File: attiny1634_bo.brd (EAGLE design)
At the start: 49.5 x 22.2 mm, 11 parts, among them J1 AVR_SPI_PRG_6NS, Y1 16MHz

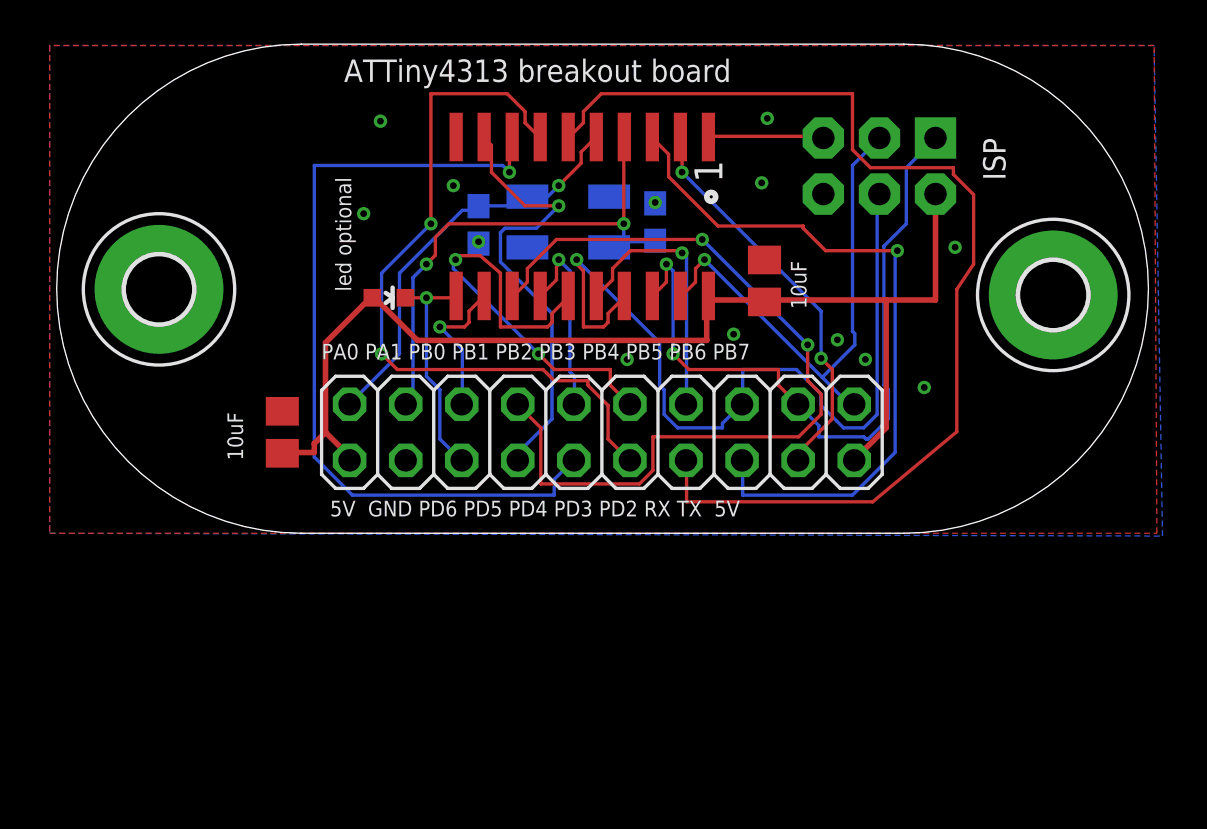
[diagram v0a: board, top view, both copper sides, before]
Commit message: use the new part and remove old wires from schematic
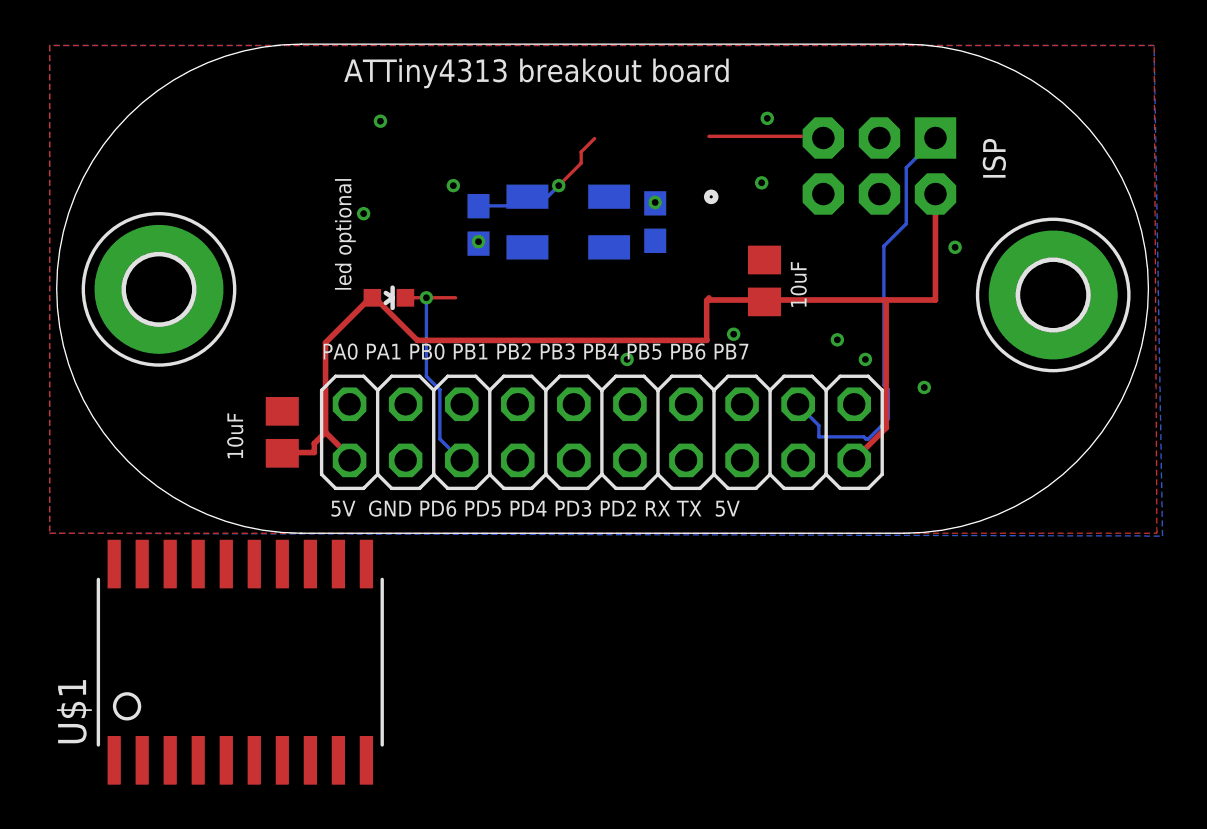
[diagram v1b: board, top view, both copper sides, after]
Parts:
- U$1: value ATTINY2313A -> ATTINY1634; device SparkFun-DigitalIC:SOP20 -> attiny1634:SOIC20
- moved U$1 36.0 mm to (-0.25, -12.2), turned to 0 degrees
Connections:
- removed net PA0/XTAL1: CX0.2, JP1.19, U$1.5, Y1.3
- removed net PA1/XTAL2: CX1.2, JP1.17, U$1.4, Y1.1
- removed net PA2/RESET-: J1.5, U$1.1
- removed net PB0: JP1.15, U$1.12
- removed net PB1: JP1.13, U$1.13
- removed net PB2: JP1.11, U$1.14
- removed net PB3: JP1.9, U$1.15
- removed net PB4: JP1.7, U$1.16
- removed net PB5/MOSI: J1.4, JP1.5, U$1.17
- removed net PB7/SCL: J1.3, JP1.1, U$1.19
- removed net PD0/RDX: JP1.4, U$1.2
- removed net PD1/TXD: JP1.6, U$1.3
- removed net PD2: JP1.8, U$1.6
- removed net PD3: JP1.10, U$1.7
- removed net PD4: JP1.12, U$1.8
- removed net PD5: JP1.14, U$1.9
- new net N$11: CX0.2, Y1.3
- new net N$3: J1.5
- new net N$4: J1.4
- new net N$7: J1.3
- new net N$9: CX1.2, Y1.1
- new net VCC: U$1.11
- net +5V: no longer U$1.20
- net PB6/MISO: no longer JP1.3, U$1.18
- net PD6: no longer JP1.16, U$1.11
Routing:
- net PD2: track 49.3 -> 0.00 mm
- net PB1: track 39.1 -> 0.00 mm, vias 2 -> 0
- net PB5/MOSI: track 38.2 -> 0.00 mm, vias 1 -> 0
- net PD4: track 37.4 -> 0.00 mm, vias 1 -> 0
- net PD3: track 33.0 -> 0.00 mm, vias 2 -> 0
- net PD1/TXD: track 32.4 -> 0.00 mm, vias 1 -> 0
- net PA1/XTAL2: track 24.7 -> 0.00 mm, vias 2 -> 0
- net PB7/SCL: track 23.6 -> 0.00 mm, vias 1 -> 0
- net PD5: track 20.5 -> 0.00 mm, vias 1 -> 0
- net PB3: track 20.3 -> 0.00 mm, vias 2 -> 0
- net PA0/XTAL1: track 19.0 -> 0.00 mm, vias 1 -> 0
- net PD0/RDX: track 18.1 -> 0.00 mm, vias 2 -> 0
- net PB6/MISO: track 32.1 -> 19.1 mm, vias 2 -> 0
- net PB4: track 12.1 -> 0.00 mm, vias 1 -> 0
- net PB2: track 8.85 -> 0.00 mm, vias 1 -> 0
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
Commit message: 12MHz max speed for this part
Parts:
- Y1: value 16MHz -> 12MHz
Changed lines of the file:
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@@
 <element name="CX0" library="rcl" package="C0603" value="22pF" x="19.431" y="13.97" smashed="yes" rot="MR90"/>
 <element name="CX1" library="rcl" package="C0603" value="22pF" x="27.432" y="14.097" smashed="yes" rot="MR270"/>
-<element name="Y1" library="SparkFun-FreqCtrl" package="CRYSTAL-SMD-5X3" value="16MHz" x="23.495" y="14.097" smashed="yes" rot="MR0"/>
+<element name="Y1" library="SparkFun-FreqCtrl" package="CRYSTAL-SMD-5X3" value="12MHz" x="23.495" y="14.097" smashed="yes" rot="MR0"/>
 <element name="H1" library="holes" package="3,0-PAD" value="MOUNT-PAD-ROUND3.0" x="4.953" y="11.049"/>
 <element name="H2" library="holes" package="3,0-PAD" value="MOUNT-PAD-ROUND3.0" x="45.466" y="10.795"/>

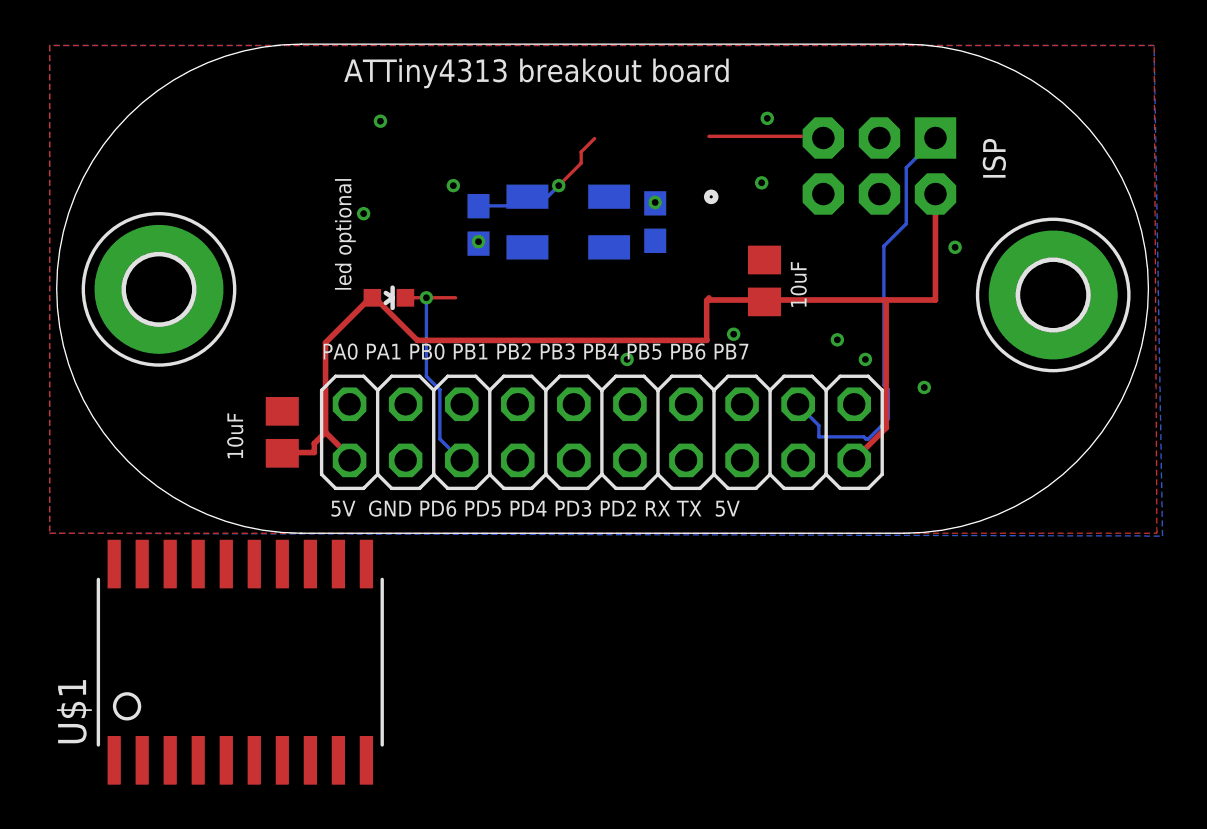
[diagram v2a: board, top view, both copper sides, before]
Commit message: ripup the traces, needs to be rerouted anyway
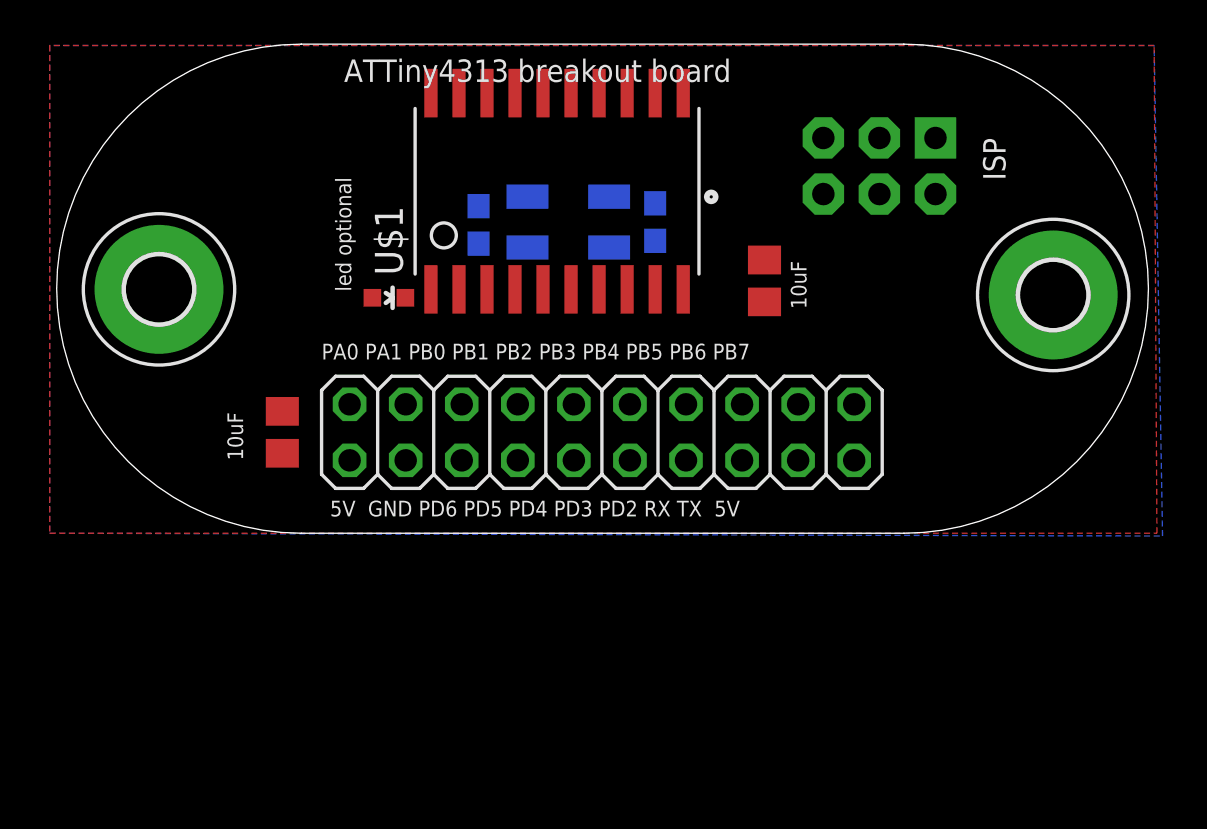
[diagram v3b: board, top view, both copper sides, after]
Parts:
- moved U$1 25.7 mm to (14.1, 9.14)
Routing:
- net +5V: track 52.3 -> 0.00 mm
- net PB6/MISO: track 19.1 -> 0.00 mm
- net PD6: track 10.2 -> 0.00 mm, vias 1 -> 0
- net N$11: track 7.06 -> 0.00 mm, vias 1 -> 0
- net N$3: track 5.26 -> 0.00 mm
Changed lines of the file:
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@@
 <attribute name="VALUE" x="37.719" y="9.017" size="1.27" layer="27" rot="R180"/>
 </element>
-<element name="U$1" library="attiny1634" package="SOIC20" value="ATTINY1634" x="-0.254" y="-12.192"/>
+<element name="U$1" library="attiny1634" package="SOIC20" value="ATTINY1634" x="14.097" y="9.144"/>
 </elements>
 <signals>
@@
 <contactref element="H2" pad="B3,0"/>
 <contactref element="JP1" pad="18"/>
-<via x="27.432" y="14.986" extent="1-16" drill="0.3048"/>
-<via x="19.431" y="13.208" extent="1-16" drill="0.3048"/>
-<via x="18.288" y="15.748" extent="1-16" drill="0.3048"/>
-<via x="35.687" y="8.763" extent="1-16" drill="0.3048"/>
-<via x="36.957" y="7.874" extent="1-16" drill="0.3048"/>
-<via x="26.162" y="7.874" extent="1-16" drill="0.3048"/>
-<via x="32.512" y="18.796" extent="1-16" drill="0.3048"/>
-<via x="41.021" y="12.954" extent="1-16" drill="0.3048"/>
-<via x="39.624" y="6.604" extent="1-16" drill="0.3048"/>
-<via x="32.258" y="15.875" extent="1-16" drill="0.3048"/>
-<via x="14.986" y="18.669" extent="1-16" drill="0.3048"/>
-<via x="14.224" y="14.478" extent="1-16" drill="0.3048"/>
-<via x="30.988" y="9.017" extent="1-16" drill="0.3048"/>
 <contactref element="U$1" pad="10"/>
-<wire x1="41.021" y1="12.954" x2="45.466" y2="10.795" width="0" layer="19" extent="1-1"/>
-<wire x1="35.052" y1="15.367" x2="41.021" y2="12.954" width="0" layer="19" extent="1-1"/>
-<wire x1="32.258" y1="15.875" x2="35.052" y2="15.367" width="0" layer="19" extent="1-1"/>
-<wire x1="32.512" y1="18.796" x2="32.258" y2="15.875" width="0" layer="19" extent="1-1"/>
-<wire x1="32.385" y1="12.38" x2="32.258" y2="15.875" width="0" layer="19" extent="1-1"/>
-<wire x1="30.988" y1="9.017" x2="32.385" y2="12.38" width="0" layer="19" extent="1-1"/>
-<wire x1="35.687" y1="8.763" x2="30.988" y2="9.017" width="0" layer="19" extent="1-1"/>
-<wire x1="36.957" y1="7.874" x2="35.687" y2="8.763" width="0" layer="19" extent="1-1"/>
-<wire x1="39.624" y1="6.604" x2="36.957" y2="7.874" width="0" layer="19" extent="1-1"/>
-<wire x1="27.432" y1="14.947" x2="32.258" y2="15.875" width="0" layer="19" extent="16-16"/>
-<wire x1="27.432" y1="14.986" x2="27.432" y2="14.947" width="0" layer="19" extent="16-16"/>
-<wire x1="26.162" y1="7.874" x2="30.988" y2="9.017" width="0" layer="19" extent="1-1"/>
-<wire x1="19.431" y1="13.208" x2="27.432" y2="14.947" width="0" layer="19" extent="16-16"/>
-<wire x1="19.431" y1="13.12" x2="19.431" y2="13.208" width="0" layer="19" extent="16-16"/>
-<wire x1="18.288" y1="15.748" x2="19.431" y2="13.208" width="0" layer="19" extent="1-1"/>
-<wire x1="14.224" y1="14.478" x2="18.288" y2="15.748" width="0" layer="19" extent="1-1"/>
-<wire x1="14.986" y1="18.669" x2="14.224" y2="14.478" width="0" layer="19" extent="1-1"/>
-<wire x1="10.541" y1="5.522" x2="14.224" y2="14.478" width="0" layer="19" extent="1-1"/>
-<wire x1="16.129" y1="3.302" x2="10.541" y2="5.522" width="0" layer="19" extent="1-1"/>
+<wire x1="35.052" y1="15.367" x2="45.466" y2="10.795" width="0" layer="19" extent="1-1"/>
+<wire x1="32.385" y1="12.38" x2="35.052" y2="15.367" width="0" layer="19" extent="1-1"/>
+<wire x1="28.702" y1="11.049" x2="32.385" y2="12.38" width="0" layer="19" extent="1-1"/>
+<wire x1="27.432" y1="14.947" x2="28.702" y2="11.049" width="0" layer="19" extent="1-16"/>
+<wire x1="19.431" y1="13.12" x2="27.432" y2="14.947" width="0" layer="19" extent="16-16"/>
+<wire x1="16.129" y1="3.302" x2="19.431" y2="13.12" width="0" layer="19" extent="16-16"/>
+<wire x1="10.541" y1="5.522" x2="16.129" y2="3.302" width="0" layer="19" extent="1-1"/>
 <wire x1="4.953" y1="11.049" x2="10.541" y2="5.522" width="0" layer="19" extent="1-1"/>
-<wire x1="14.351" y1="-10.287" x2="16.129" y2="3.302" width="0" layer="19" extent="1-1"/>
 </signal>
 <signal name="+5V" class="1">
@@
 <contactref element="JP1" pad="2"/>
 <contactref element="JP1" pad="20"/>
-<wire x1="12.4968" y1="8.636" x2="14.5288" y2="10.668" width="0.254" layer="1"/>
-<wire x1="12.4968" y1="4.572" x2="12.4968" y2="8.636" width="0.254" layer="1"/>
-<wire x1="13.5128" y1="3.556" x2="12.4968" y2="4.572" width="0.254" layer="1"/>
-<wire x1="13.5128" y1="3.3528" x2="13.5128" y2="3.556" width="0.254" layer="1"/>
-<wire x1="14.5288" y1="10.668" x2="14.617" y2="10.668" width="0.254" layer="1"/>
-<wire x1="13.5128" y1="3.3528" x2="13.589" y2="3.302" width="0.254" layer="1"/>
-<wire x1="11.9888" y1="3.6576" x2="10.5664" y2="3.6576" width="0.254" layer="1"/>
-<wire x1="11.9888" y1="4.064" x2="11.9888" y2="3.6576" width="0.254" layer="1"/>
-<wire x1="12.3952" y1="4.4704" x2="11.9888" y2="4.064" width="0.254" layer="1"/>
-<wire x1="12.3952" y1="4.572" x2="12.3952" y2="4.4704" width="0.254" layer="1"/>
-<wire x1="10.5664" y1="3.6576" x2="10.541" y2="3.622" width="0.254" layer="1"/>
-<wire x1="12.3952" y1="4.572" x2="12.4968" y2="4.572" width="0.254" layer="1"/>
-<wire x1="29.8704" y1="10.5664" x2="32.3088" y2="10.5664" width="0.254" layer="1"/>
-<wire x1="29.8704" y1="10.668" x2="29.8704" y2="10.5664" width="0.254" layer="1"/>
-<wire x1="32.3088" y1="10.5664" x2="32.385" y2="10.48" width="0.254" layer="1"/>
-<wire x1="40.132" y1="10.5664" x2="37.8968" y2="10.5664" width="0.254" layer="1"/>
-<wire x1="37.8968" y1="10.5664" x2="32.4104" y2="10.5664" width="0.254" layer="1"/>
-<wire x1="40.132" y1="15.367" x2="40.132" y2="10.5664" width="0.254" layer="1"/>
-<wire x1="32.4104" y1="10.5664" x2="32.385" y2="10.48" width="0.254" layer="1"/>
-<wire x1="37.8968" y1="4.7752" x2="36.4744" y2="3.3528" width="0.254" layer="1"/>
-<wire x1="37.8968" y1="10.5664" x2="37.8968" y2="4.7752" width="0.254" layer="1"/>
-<wire x1="36.4744" y1="3.3528" x2="36.449" y2="3.302" width="0.254" layer="1"/>
-<wire x1="16.6624" y1="8.7376" x2="14.732" y2="10.668" width="0.254" layer="1"/>
-<wire x1="29.7688" y1="8.7376" x2="16.6624" y2="8.7376" width="0.254" layer="1"/>
-<wire x1="29.7688" y1="10.5664" x2="29.7688" y2="8.7376" width="0.254" layer="1"/>
-<wire x1="14.732" y1="10.668" x2="14.617" y2="10.668" width="0.254" layer="1"/>
-<wire x1="29.7688" y1="10.5664" x2="29.8704" y2="10.5664" width="0" layer="19" extent="1-1"/>
+<wire x1="32.385" y1="10.48" x2="40.132" y2="15.367" width="0" layer="19" extent="1-1"/>
+<wire x1="36.449" y1="3.302" x2="32.385" y2="10.48" width="0" layer="19" extent="1-1"/>
+<wire x1="14.617" y1="10.668" x2="32.385" y2="10.48" width="0" layer="19" extent="1-1"/>
+<wire x1="13.589" y1="3.302" x2="14.617" y2="10.668" width="0" layer="19" extent="1-1"/>
+<wire x1="10.541" y1="3.622" x2="13.589" y2="3.302" width="0" layer="19" extent="1-1"/>
 </signal>
 <signal name="PB6/MISO">
 <contactref element="J1" pad="1"/>
-<wire x1="38.8112" y1="16.5608" x2="40.132" y2="17.8816" width="0.1524" layer="16"/>
-<wire x1="38.8112" y1="14.0208" x2="38.8112" y2="16.5608" width="0.1524" layer="16"/>
-<wire x1="37.7952" y1="13.0048" x2="38.8112" y2="14.0208" width="0.1524" layer="16"/>
-<wire x1="37.7952" y1="6.7056" x2="37.7952" y2="13.0048" width="0.1524" layer="16"/>
-<wire x1="37.9984" y1="6.5024" x2="37.7952" y2="6.7056" width="0.1524" layer="16"/>
-<wire x1="37.9984" y1="5.1816" x2="37.9984" y2="6.5024" width="0.1524" layer="16"/>
-<wire x1="37.084" y1="4.2672" x2="37.9984" y2="5.1816" width="0.1524" layer="16"/>
-<wire x1="36.9824" y1="4.2672" x2="37.084" y2="4.2672" width="0.1524" layer="16"/>
-<wire x1="36.8808" y1="4.3688" x2="36.9824" y2="4.2672" width="0.1524" layer="16"/>
-<wire x1="34.8488" y1="4.3688" x2="36.8808" y2="4.3688" width="0.1524" layer="16"/>
-<wire x1="34.8488" y1="4.8768" x2="34.8488" y2="4.3688" width="0.1524" layer="16"/>
-<wire x1="33.9344" y1="5.7912" x2="34.8488" y2="4.8768" width="0.1524" layer="16"/>
-<wire x1="40.132" y1="17.8816" x2="40.132" y2="17.907" width="0.1524" layer="16"/>
 </signal>
 <signal name="PD6">
 <contactref element="LED1" pad="C"/>
-<wire x1="18.3896" y1="10.668" x2="17.0688" y2="10.668" width="0.1524" layer="1"/>
-<wire x1="17.0688" y1="10.668" x2="16.117" y2="10.668" width="0.1524" layer="1"/>
-<wire x1="17.0688" y1="7.112" x2="17.0688" y2="10.668" width="0.1524" layer="16"/>
-<wire x1="17.6784" y1="6.5024" x2="17.0688" y2="7.112" width="0.1524" layer="16"/>
-<wire x1="17.6784" y1="4.2672" x2="17.6784" y2="6.5024" width="0.1524" layer="16"/>
-<wire x1="18.5928" y1="3.3528" x2="17.6784" y2="4.2672" width="0.1524" layer="16"/>
-<via x="17.0688" y="10.668" extent="1-16" drill="0.3048"/>
 </signal>
 <signal name="N$3">
 <contactref element="J1" pad="5"/>
-<wire x1="35.052" y1="17.9832" x2="29.8704" y2="17.9832" width="0.1524" layer="1"/>
-<wire x1="35.052" y1="17.9832" x2="35.052" y2="17.907" width="0.1524" layer="1"/>
 </signal>
 <signal name="N$4">
@@
 <contactref element="CX0" pad="2"/>
 <contactref element="Y1" pad="3"/>
-<wire x1="21.6408" y1="14.8336" x2="19.5072" y2="14.8336" width="0.1524" layer="16"/>
-<wire x1="21.6408" y1="15.24" x2="21.6408" y2="14.8336" width="0.1524" layer="16"/>
-<wire x1="19.5072" y1="14.8336" x2="19.431" y2="14.82" width="0.1524" layer="16"/>
-<wire x1="21.6408" y1="15.24" x2="21.645" y2="15.247" width="0.1524" layer="16"/>
-<wire x1="24.0792" y1="17.272" x2="24.6888" y2="17.8816" width="0.1524" layer="1"/>
-<wire x1="24.0792" y1="16.764" x2="24.0792" y2="17.272" width="0.1524" layer="1"/>
-<wire x1="23.0632" y1="15.748" x2="24.0792" y2="16.764" width="0.1524" layer="1"/>
-<wire x1="22.5552" y1="15.24" x2="23.0632" y2="15.748" width="0.1524" layer="16"/>
-<wire x1="21.7424" y1="15.24" x2="22.5552" y2="15.24" width="0.1524" layer="16"/>
-<wire x1="21.7424" y1="15.24" x2="21.645" y2="15.247" width="0.1524" layer="16"/>
-<via x="23.0632" y="15.748" extent="1-16" drill="0.3048"/>
+<wire x1="19.431" y1="14.82" x2="21.645" y2="15.247" width="0" layer="19" extent="16-16"/>
 </signal>
 <signal name="VCC">
